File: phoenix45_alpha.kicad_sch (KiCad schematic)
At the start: 114 parts, among them SW1 SW_PUSH, SW2 SW_PUSH, U1 SRV05-4, U3 ATmega32U4-M, X1 Crystal_GND24_Small

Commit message: v1
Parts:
- U3: footprint Package_DFN_QFN:QFN-44-1EP_7x7mm_P0.5mm_EP5.2x5.2mm -> Package_DFN_QFN:QFN-44-1EP_7x7mm_P0.5mm_EP5.2x5.2mm_ThermalVias
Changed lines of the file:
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@@
   (junction (at 99.06 194.31) (diameter 0) (color 0 0 0 0)
   )
-  (junction (at 115.57 55.88) (diameter 0) (color 0 0 0 0)
-  )
   (junction (at 22.86 115.57) (diameter 0) (color 0 0 0 0)
   )
@@
     (stroke (width 0) (type default) (color 0 0 0 0))
   )
-  (wire (pts (xy 115.57 55.88) (xy 115.57 57.15))
-    (stroke (width 0) (type default) (color 0 0 0 0))
-  )
   (wire (pts (xy 99.06 194.31) (xy 124.46 194.31))
     (stroke (width 0) (type default) (color 0 0 0 0))
@@
     (stroke (width 0) (type default) (color 0 0 0 0))
   )
+  (wire (pts (xy 115.57 57.15) (xy 116.205 57.15))
+    (stroke (width 0) (type default) (color 0 0 0 0))
+  )
   (wire (pts (xy 140.97 209.55) (xy 140.97 234.95))
     (stroke (width 0) (type default) (color 0 0 0 0))
@@
     (stroke (width 0) (type default) (color 0 0 0 0))
   )
+  (wire (pts (xy 116.205 57.15) (xy 116.205 55.88))
+    (stroke (width 0) (type default) (color 0 0 0 0))
+  )
   (wire (pts (xy 151.13 234.95) (xy 149.86 234.95))
     (stroke (width 0) (type default) (color 0 0 0 0))
@@
       (effects (font (size 1.27 1.27)) (justify left))
     )
-    (property "Footprint" "Package_DFN_QFN:QFN-44-1EP_7x7mm_P0.5mm_EP5.2x5.2mm" (id 2) (at 142.24 93.98 0)
+    (property "Footprint" "Package_DFN_QFN:QFN-44-1EP_7x7mm_P0.5mm_EP5.2x5.2mm_ThermalVias" (id 2) (at 142.24 93.98 0)
       (effects (font (size 1.27 1.27) italic) hide)
     )
@@
     )
     (path "/fe1a8f1c-b239-442d-acdc-13f4ebc5e42a"
-      (reference "U3") (unit 1) (value "ATmega32U4-M") (footprint "Package_DFN_QFN:QFN-44-1EP_7x7mm_P0.5mm_EP5.2x5.2mm")
+      (reference "U3") (unit 1) (value "ATmega32U4-M") (footprint "Package_DFN_QFN:QFN-44-1EP_7x7mm_P0.5mm_EP5.2x5.2mm_ThermalVias")
     )
     (path "/5f7b6686-ca41-45e8-807e-4d2ae5a4c66e"

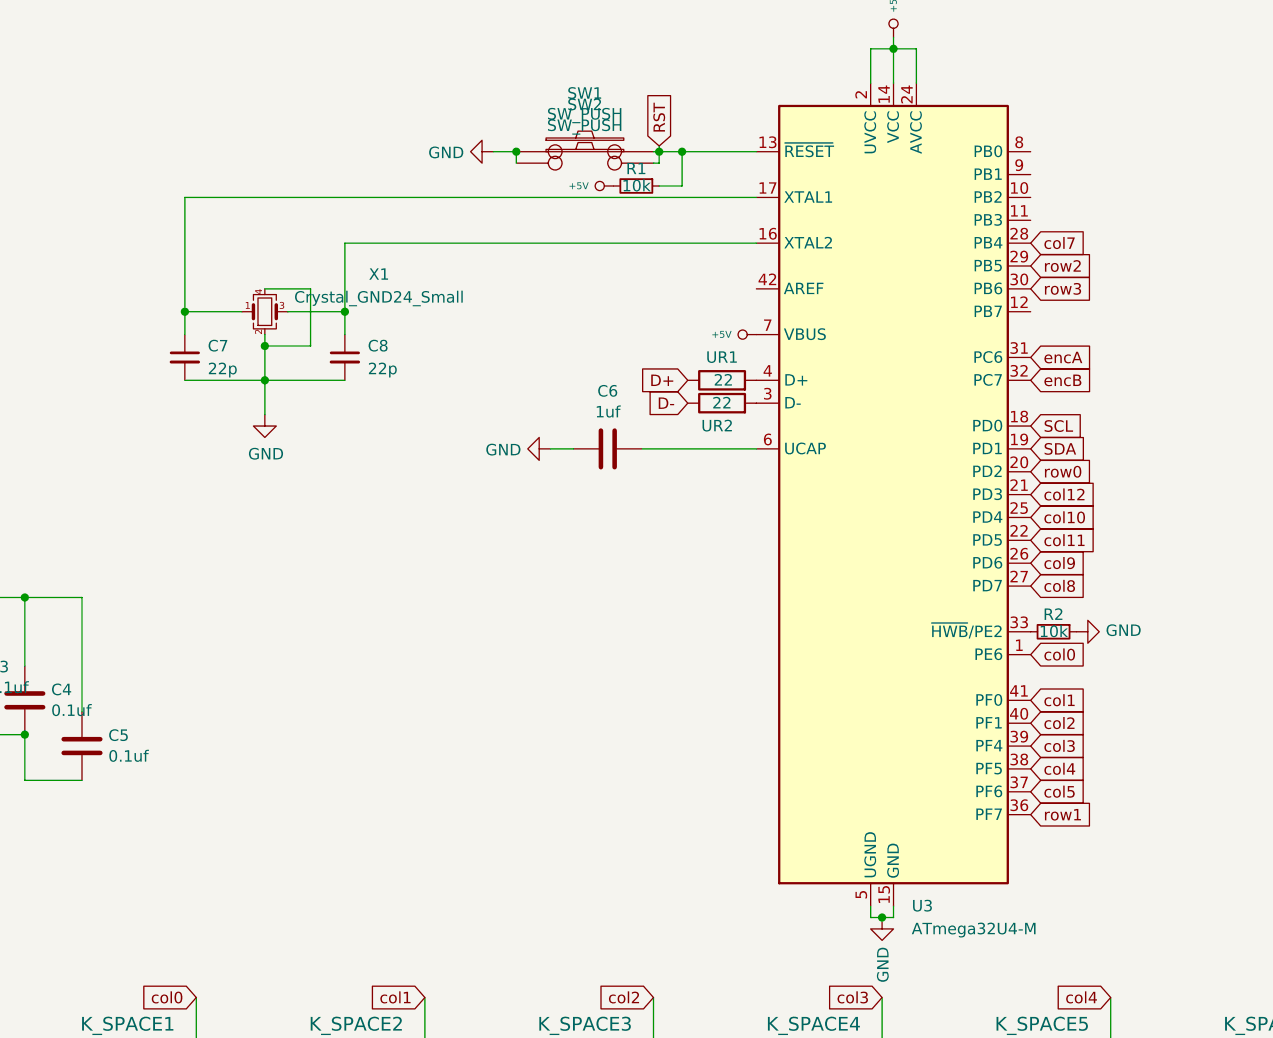
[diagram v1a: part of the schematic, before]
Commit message: added avr
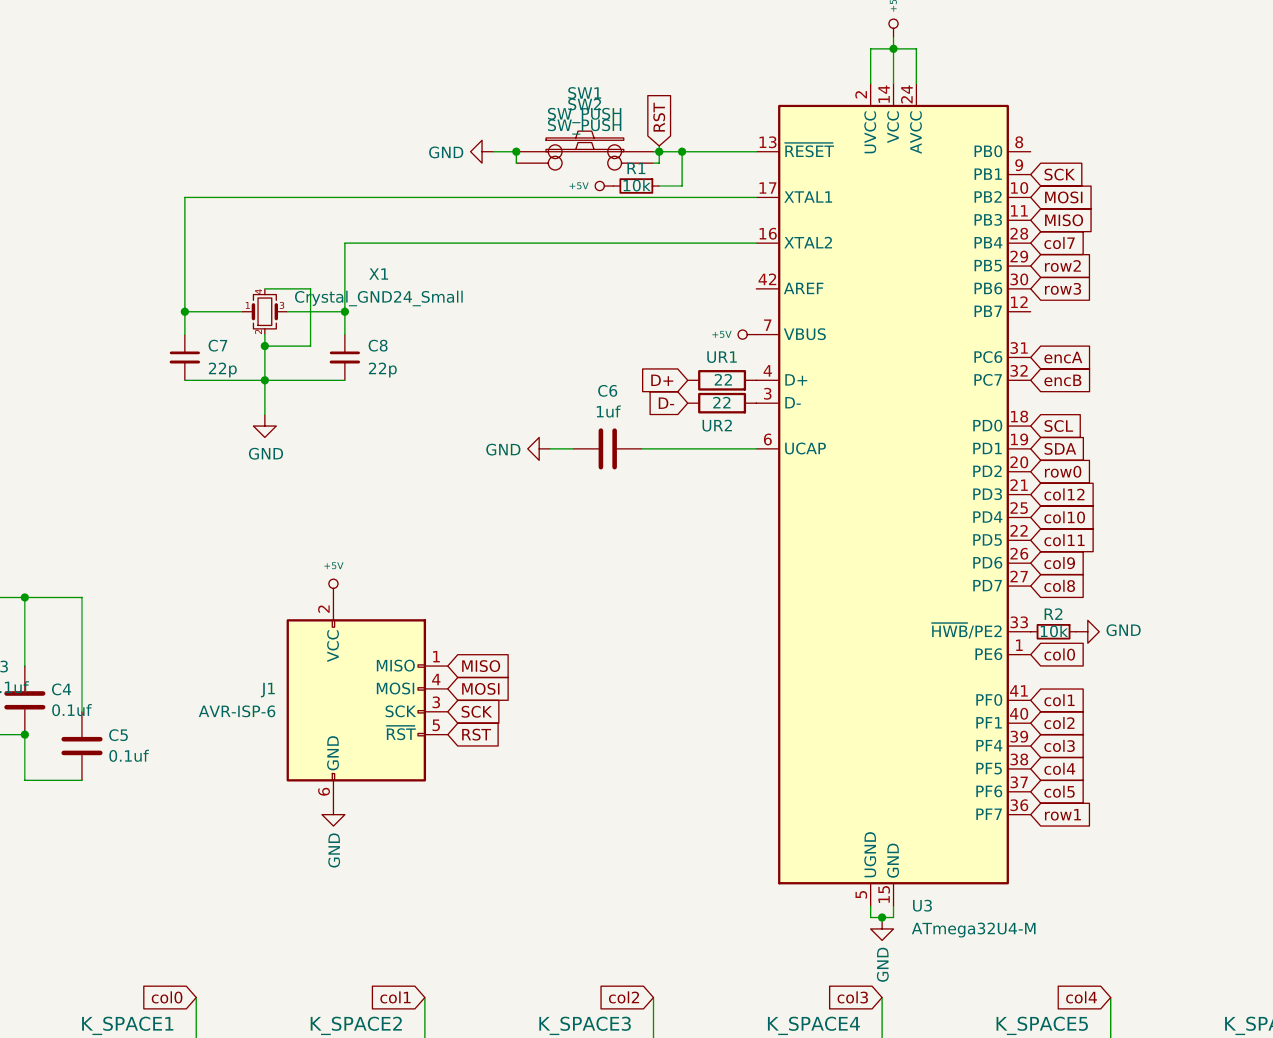
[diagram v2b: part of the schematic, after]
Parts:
- added J1: AVR-ISP-6, Connector_IDC:IDC-Header_2x03_P2.54mm_Vertical, symbol Connector:AVR-ISP-6
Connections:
- net +5V: now also J1.2 (VCC)
- net GND: now also J1.6 (GND)
- net RST: now also J1.5 (~{RST})
- net MOSI: now reaches U3.10 (PB2)
- net MOSI: now also J1.4 (MOSI)
- net MISO: now reaches U3.11 (PB3)
- net MISO: now also J1.1 (MISO)
- net SCK: now reaches U3.9 (PB1)
- net SCK: now also J1.3 (SCK)
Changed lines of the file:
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@@
+    )
+  )
+  (global_label "MOSI" (shape input) (at 92.71 115.57 0) (fields_autoplaced)
+    (effects (font (size 1.27 1.27)) (justify left))
+    (property "Intersheet References" "${INTERSHEET_REFS}" (id 0) (at 99.6304 115.4906 0)
+      (effects (font (size 1.27 1.27)) (justify left) hide)
     )
   )
@@
     )
   )
+  (global_label "SCK" (shape input) (at 157.48 58.42 0) (fields_autoplaced)
+    (effects (font (size 1.27 1.27)) (justify left))
+    (property "Intersheet References" "${INTERSHEET_REFS}" (id 0) (at 163.5537 58.3406 0)
+      (effects (font (size 1.27 1.27)) (justify left) hide)
+    )
+  )
   (global_label "col9" (shape input) (at 293.37 149.86 180) (fields_autoplaced)
     (effects (font (size 1.27 1.27)) (justify right))
     (property "Intersheet References" "${INTERSHEET_REFS}" (id 0) (at 19.05 133.35 0)
       (effects (font (size 1.27 1.27)) hide)
+    )
+  )
+  (global_label "MISO" (shape input) (at 157.48 63.5 0) (fields_autoplaced)
+    (effects (font (size 1.27 1.27)) (justify left))
+    (property "Intersheet References" "${INTERSHEET_REFS}" (id 0) (at 164.4004 63.4206 0)
+      (effects (font (size 1.27 1.27)) (justify left) hide)
     )
   )
@@
     )
   )
+  (global_label "RST" (shape input) (at 92.71 120.65 0) (fields_autoplaced)
+    (effects (font (size 1.27 1.27)) (justify left))
+    (property "Intersheet References" "${INTERSHEET_REFS}" (id 0) (at 433.705 -424.18 0)
+      (effects (font (size 1.27 1.27)) hide)
+    )
+  )
+  (global_label "SCK" (shape input) (at 92.71 118.11 0) (fields_autoplaced)
+    (effects (font (size 1.27 1.27)) (justify left))
+    (property "Intersheet References" "${INTERSHEET_REFS}" (id 0) (at 98.7837 118.0306 0)
+      (effects (font (size 1.27 1.27)) (justify left) hide)
+    )
+  )
   (global_label "col7" (shape input) (at 242.57 149.86 180) (fields_autoplaced)
     (effects (font (size 1.27 1.27)) (justify right))
@@
     )
   )
+  (global_label "MISO" (shape input) (at 92.71 113.03 0) (fields_autoplaced)
+    (effects (font (size 1.27 1.27)) (justify left))
+    (property "Intersheet References" "${INTERSHEET_REFS}" (id 0) (at 99.6304 112.9506 0)
+      (effects (font (size 1.27 1.27)) (justify left) hide)
+    )
+  )
   (global_label "RST" (shape input) (at 116.205 55.245 90) (fields_autoplaced)
     (effects (font (size 1.27 1.27)) (justify left))
@@
     (property "Intersheet References" "${INTERSHEET_REFS}" (id 0) (at 19.05 133.35 0)
       (effects (font (size 1.27 1.27)) hide)
+    )
+  )
+  (global_label "MOSI" (shape input) (at 157.48 60.96 0) (fields_autoplaced)
+    (effects (font (size 1.27 1.27)) (justify left))
+    (property "Intersheet References" "${INTERSHEET_REFS}" (id 0) (at 164.4004 60.8806 0)
+      (effects (font (size 1.27 1.27)) (justify left) hide)
     )
   )
@@
     (pin "2")
   )
+  (symbol (lib_id "keyboard_parts:+5V") (at 80.01 105.41 0) (unit 1)
+    (in_bom yes) (on_board yes)
+    (property "Reference" "#PWR0112" (id 0) (at 80.01 106.172 0)
+      (effects (font (size 0.508 0.508)) hide)
+    )
+    (property "Value" "+5V" (id 1) (at 80.01 101.9048 0)
+      (effects (font (size 0.762 0.762)))
+    )
+    (property "Footprint" "" (id 2) (at 80.01 105.41 0)
+      (effects (font (size 1.524 1.524)))
+    )
+    (property "Datasheet" "" (id 3) (at 80.01 105.41 0)
+      (effects (font (size 1.524 1.524)))
+    )
+    (pin "1")
+  )
   (symbol (lib_id "keyboard_parts:KEYSW") (at 285.75 234.95 0) (unit 1)
     (in_bom yes) (on_board yes)
@@
     (pin "1")
     (pin "2")
+  )
+  (symbol (lib_id "Connector:AVR-ISP-6") (at 82.55 118.11 0) (unit 1)
+    (in_bom yes) (on_board yes) (fields_autoplaced)
+    (property "Reference" "J1" (id 0) (at 73.66 115.5699 0)
+      (effects (font (size 1.27 1.27)) (justify right))
+    )
+    (property "Value" "AVR-ISP-6" (id 1) (at 73.66 118.1099 0)
+      (effects (font (size 1.27 1.27)) (justify right))
+    )
+    (property "Footprint" "Connector_IDC:IDC-Header_2x03_P2.54mm_Vertical" (id 2) (at 76.2 116.84 90)
+      (effects (font (size 1.27 1.27)) hide)
+    )
+    (property "Datasheet" " ~" (id 3) (at 50.165 132.08 0)
+      (effects (font (size 1.27 1.27)) hide)
+    )
+    (pin "1")
+    (pin "2")
+    (pin "3")
+    (pin "4")
+    (pin "5")
+    (pin "6")
   )
   (symbol (lib_id "Type-C:HRO-TYPE-C-31-M-12") (at 216.535 76.2 0) (unit 1)
@@
     (pin "1")
     (pin "2")
+  )
+  (symbol (lib_id "power:GND") (at 80.01 128.27 0) (unit 1)
+    (in_bom yes) (on_board yes)
+    (property "Reference" "#PWR0113" (id 0) (at 80.01 134.62 0)
+      (effects (font (size 1.27 1.27)) hide)
+    )
+    (property "Value" "GND" (id 1) (at 80.137 131.5212 90)
+      (effects (font (size 1.27 1.27)) (justify right))
+    )
+    (property "Footprint" "" (id 2) (at 80.01 128.27 0)
+      (effects (font (size 1.27 1.27)) hide)
+    )
+    (property "Datasheet" "" (id 3) (at 80.01 128.27 0)
+      (effects (font (size 1.27 1.27)) hide)
+    )
+    (pin "1")
   )
   (symbol (lib_id "Device:D") (at 251.46 190.5 90) (unit 1)
@@
       (reference "#PWR0111") (unit 1) (value "GND") (footprint "")
     )
+    (path "/9559dcc0-2949-46ca-a852-a0c170abf61b"
+      (reference "#PWR0112") (unit 1) (value "+5V") (footprint "")
+    )
+    (path "/c2d48dd0-f303-4a06-9c6b-433733e8bb22"
+      (reference "#PWR0113") (unit 1) (value "GND") (footprint "")
+    )
     (path "/f44b8b10-6788-445e-8c02-01cabfaec13a"
       (reference "#PWR0114") (unit 1) (value "+5V") (footprint "")
@@
       (reference "F1") (unit 1) (value "Polyfuse_Small") (footprint "Fuse:Fuse_1206_3216Metric_Pad1.42x1.75mm_HandSolder")
     )
+    (path "/b6fa00f8-3f6d-476b-aebc-8e9051125776"
+      (reference "J1") (unit 1) (value "AVR-ISP-6") (footprint "Connector_IDC:IDC-Header_2x03_P2.54mm_Vertical")
+    )
     (path "/d126c263-2a4c-4321-923f-547c005a2676"

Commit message: trackpoint
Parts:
- added C9: 2.2uF, Capacitor_SMD:C_0805_2012Metric_Pad1.18x1.45mm_HandSolder, symbol device:C_Small
- added TP1: TPCLK, TestPoint:TestPoint_Pad_1.0x1.0mm, symbol Connector:TestPoint
- added TP2: TPVCC, TestPoint:TestPoint_Pad_1.0x1.0mm, symbol Connector:TestPoint
- added TP3: TPGND, TestPoint:TestPoint_Pad_1.0x1.0mm, symbol Connector:TestPoint
- added TP4: TPDATA, TestPoint:TestPoint_Pad_1.0x1.0mm, symbol Connector:TestPoint
- added TP5: TPRST, TestPoint:TestPoint_Pad_1.0x1.0mm, symbol Connector:TestPoint
- added UR6, UR7: 4.7k, Resistor_SMD:R_0805_2012Metric_Pad1.20x1.40mm_HandSolder, symbol device:R
- added UR8: 100k, Resistor_SMD:R_0805_2012Metric_Pad1.20x1.40mm_HandSolder, symbol device:R
- C0, C1, C2, C3, C4, C5, C6, C7, C8: footprint Capacitor_SMD:C_0805_2012Metric -> Capacitor_SMD:C_0805_2012Metric_Pad1.18x1.45mm_HandSolder
- R1, R2, UR1, UR2, UR3, UR4, UR5: footprint Resistor_SMD:R_0805_2012Metric -> Resistor_SMD:R_0805_2012Metric_Pad1.20x1.40mm_HandSolder
- U1: footprint Package_TO_SOT_SMD:SOT-23-6 -> Package_TO_SOT_SMD:SOT-23-6_Handsoldering
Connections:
- net encA is gone; now on net row2: U3.31 (PC6)
- net encB is gone; now on net row3: U3.32 (PC7)
- net +5V: now also C9.1, TP2.1, UR6.1, UR7.2
- net GND: now also TP3.1, UR8.2
- net col10: now also U3.27 (PD7); no longer U3.25 (PD4)
- net col11: now also U3.26 (PD6); no longer U3.22 (PD5)
- net col12: now also U3.25 (PD4); no longer U3.21 (PD3)
- net col7: now also U3.30 (PB6); no longer U3.28 (PB4)
- net col8: now also U3.29 (PB5); no longer U3.27 (PD7)
- net col9: now also U3.28 (PB4); no longer U3.26 (PD6)
- net row0: now also U3.21 (PD3); no longer U3.20 (PD2)
- net row2: no longer U3.29 (PB5)
- net row3: no longer U3.30 (PB6)
- new net: C9.2, TP5.1, UR8.1
- new net PD2: TP4.1, U3.20 (PD2), UR7.1
- new net PD5: TP1.1, U3.22 (PD5), UR6.2
